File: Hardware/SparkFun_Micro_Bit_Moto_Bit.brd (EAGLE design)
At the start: 58.4 x 76.2 mm, 51 parts, among them J1 POWER_JACKPTH_LOCK, J2 CORTEX_DEBUGPTH, U1 CY8C4245LQI-483, U2 TPS62172, U3 micro:bit, U4 DRV8835

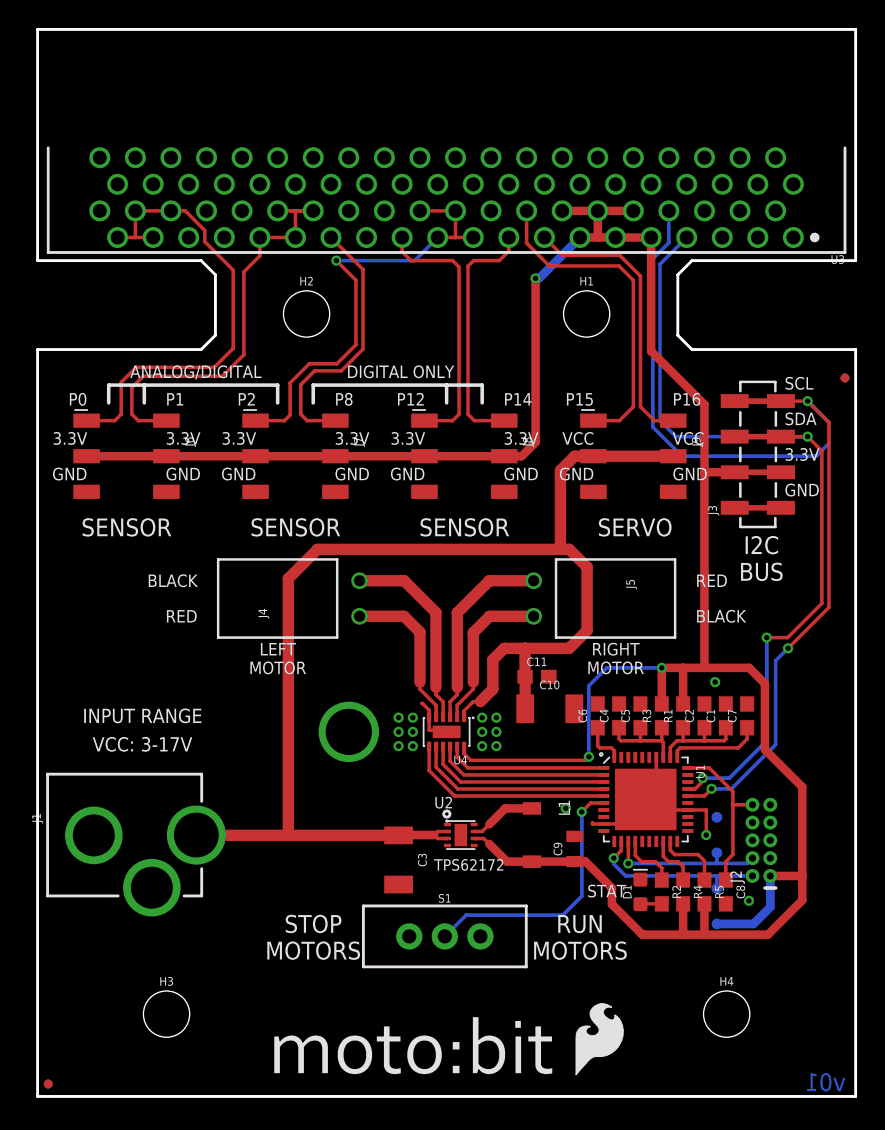
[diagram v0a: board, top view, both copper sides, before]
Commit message: Rounded Corners
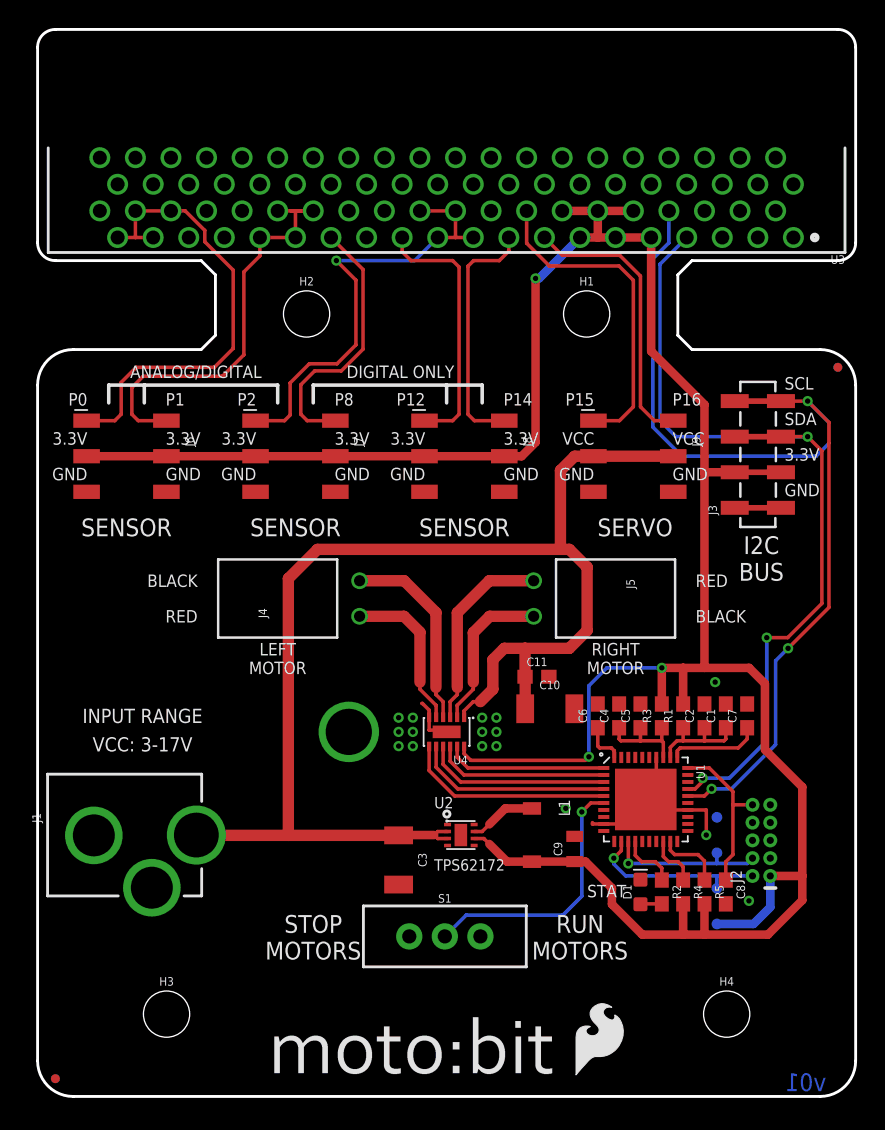
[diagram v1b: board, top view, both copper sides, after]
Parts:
- moved FD2 0.92 mm to (57.1, 52.1)
- moved FD4 0.92 mm to (57.1, 52.1)
- moved FD1 0.64 mm to (1.27, 1.27)
- moved FD3 0.64 mm to (1.27, 1.27)
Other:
- outline, holes or cut-outs redrawn
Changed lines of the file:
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@@
 <layer number="45" name="Holes" color="7" fill="1" visible="yes" active="yes"/>
 <layer number="46" name="Milling" color="3" fill="1" visible="no" active="yes"/>
-<layer number="47" name="Measures" color="7" fill="1" visible="yes" active="yes"/>
+<layer number="47" name="Measures" color="7" fill="1" visible="no" active="yes"/>
 <layer number="48" name="Document" color="7" fill="1" visible="no" active="yes"/>
 <layer number="49" name="Reference" color="7" fill="1" visible="no" active="yes"/>
@@
 <board>
 <plain>
-<wire x1="58.42" y1="0" x2="58.42" y2="53.34" width="0.2032" layer="20"/>
-<wire x1="0" y1="53.34" x2="0" y2="0" width="0.2032" layer="20"/>
+<wire x1="2.54" y1="0" x2="55.88" y2="0" width="0.2032" layer="20"/>
+<wire x1="55.88" y1="0" x2="58.42" y2="2.54" width="0.2032" layer="20" curve="90"/>
+<wire x1="46.736" y1="53.34" x2="55.88" y2="53.34" width="0.2032" layer="20"/>
+<wire x1="55.88" y1="53.34" x2="58.42" y2="50.8" width="0.2032" layer="20" curve="-90"/>
+<wire x1="58.42" y1="50.8" x2="58.42" y2="2.54" width="0.2032" layer="20"/>
+<wire x1="0" y1="2.54" x2="0" y2="50.8" width="0.2032" layer="20"/>
+<wire x1="0" y1="50.8" x2="2.54" y2="53.34" width="0.2032" layer="20" curve="-90"/>
+<wire x1="2.54" y1="53.34" x2="11.684" y2="53.34" width="0.2032" layer="20"/>
+<wire x1="0" y1="2.54" x2="2.54" y2="0" width="0.2032" layer="20" curve="90"/>
 <text x="24.13" y="-31.75" size="1.778" layer="51" font="vector" ratio="15">Alex Wende</text>
-<text x="56.261" y="0.381" size="1.27" layer="16" font="vector" ratio="15" rot="MR0" align="bottom-center">v01</text>
+<text x="54.864" y="0.381" size="1.27" layer="16" font="vector" ratio="15" rot="MR0" align="bottom-center">v01</text>
 <text x="-17.78" y="-49.53" size="1.27" layer="51" font="vector" ratio="15">- Solder mask color : Gloss Black</text>
-<wire x1="0" y1="0" x2="58.42" y2="0" width="0.2032" layer="20"/>
-<wire x1="58.42" y1="59.69" x2="46.736" y2="59.69" width="0.2032" layer="20"/>
+<wire x1="58.42" y1="74.93" x2="58.42" y2="60.96" width="0.2032" layer="20"/>
+<wire x1="58.42" y1="60.96" x2="57.15" y2="59.69" width="0.2032" layer="20" curve="-90"/>
+<wire x1="57.15" y1="59.69" x2="46.736" y2="59.69" width="0.2032" layer="20"/>
 <wire x1="46.736" y1="59.69" x2="45.72" y2="58.674" width="0.2032" layer="20"/>
 <wire x1="45.72" y1="58.674" x2="45.72" y2="54.356" width="0.2032" layer="20"/>
 <wire x1="45.72" y1="54.356" x2="46.736" y2="53.34" width="0.2032" layer="20"/>
-<wire x1="46.736" y1="53.34" x2="58.42" y2="53.34" width="0.2032" layer="20"/>
-<wire x1="0" y1="53.34" x2="11.684" y2="53.34" width="0.2032" layer="20"/>
 <wire x1="11.684" y1="53.34" x2="12.7" y2="54.356" width="0.2032" layer="20"/>
 <wire x1="12.7" y1="54.356" x2="12.7" y2="58.674" width="0.2032" layer="20"/>
 <wire x1="12.7" y1="58.674" x2="11.684" y2="59.69" width="0.2032" layer="20"/>
-<wire x1="11.684" y1="59.69" x2="0" y2="59.69" width="0.2032" layer="20"/>
-<wire x1="0" y1="59.69" x2="0" y2="76.2" width="0.2032" layer="20"/>
-<wire x1="0" y1="76.2" x2="58.42" y2="76.2" width="0.2032" layer="20"/>
-<wire x1="58.42" y1="76.2" x2="58.42" y2="59.69" width="0.2032" layer="20"/>
+<wire x1="11.684" y1="59.69" x2="1.27" y2="59.69" width="0.2032" layer="20"/>
+<wire x1="1.27" y1="59.69" x2="0" y2="60.96" width="0.2032" layer="20" curve="-90"/>
+<wire x1="0" y1="60.96" x2="0" y2="74.93" width="0.2032" layer="20"/>
+<wire x1="0" y1="74.93" x2="1.27" y2="76.2" width="0.2032" layer="20" curve="-90"/>
+<wire x1="1.27" y1="76.2" x2="57.15" y2="76.2" width="0.2032" layer="20"/>
+<wire x1="57.15" y1="76.2" x2="58.42" y2="74.93" width="0.2032" layer="20" curve="-90"/>
 <text x="3.556" y="49.784" size="0.889" layer="21" font="vector" ratio="15" rot="R180" align="center-left">P0</text>
 <text x="9.144" y="49.784" size="0.889" layer="21" font="vector" ratio="15" align="center-left">P1</text>
@@
 <element name="LOGO1" library="SparkFun-Aesthetics" package="SFE_LOGO_NAME_FLAME_.3" value="SFE_LOGO_NAME_FLAME.3_INCH" x="46.99" y="41.91" rot="MR0"/>
 <element name="LOGO2" library="SparkFun-Aesthetics" package="OSHW-LOGO-L" value="OSHW-LOGOL" x="29.083" y="6.477" rot="MR0"/>
-<element name="FD1" library="SparkFun-Aesthetics" package="FIDUCIAL-MICRO" value="FIDUCIALUFIDUCIAL" x="0.762" y="0.889"/>
-<element name="FD2" library="SparkFun-Aesthetics" package="FIDUCIAL-MICRO" value="FIDUCIALUFIDUCIAL" x="57.658" y="51.308"/>
+<element name="FD1" library="SparkFun-Aesthetics" package="FIDUCIAL-MICRO" value="FIDUCIALUFIDUCIAL" x="1.27" y="1.27"/>
+<element name="FD2" library="SparkFun-Aesthetics" package="FIDUCIAL-MICRO" value="FIDUCIALUFIDUCIAL" x="57.15" y="52.07"/>
 <element name="U1" library="SparkFun-IC-Microcontroller" package="QFN-40" value="CY8C4245LQI-483" x="43.434" y="21.209" rot="R270">
 <attribute name="PROD_ID" value="IC-13292" x="-8.636" y="107.569" size="1.778" layer="27" font="vector" ratio="15" rot="R270" display="off"/>
@@
 <element name="H3" library="SparkFun-Hardware" package="STAND-OFF" value="STAND-OFF" x="9.21" y="5.88"/>
 <element name="H4" library="SparkFun-Hardware" package="STAND-OFF" value="STAND-OFF" x="49.21" y="5.88"/>
-<element name="FD3" library="SparkFun-Aesthetics" package="FIDUCIAL-MICRO" value="FIDUCIALUFIDUCIAL" x="0.762" y="0.889" rot="MR0"/>
-<element name="FD4" library="SparkFun-Aesthetics" package="FIDUCIAL-MICRO" value="FIDUCIALUFIDUCIAL" x="57.658" y="51.308" rot="MR0"/>
+<element name="FD3" library="SparkFun-Aesthetics" package="FIDUCIAL-MICRO" value="FIDUCIALUFIDUCIAL" x="1.27" y="1.27" rot="MR0"/>
+<element name="FD4" library="SparkFun-Aesthetics" package="FIDUCIAL-MICRO" value="FIDUCIALUFIDUCIAL" x="57.15" y="52.07" rot="MR0"/>
 <element name="J9" library="SparkFun-Connectors" package="2X3_SMD" value="" x="42.545" y="45.72" rot="R270">
 <attribute name="PROD_ID" value="CONN-11290" x="-100.965" y="190.5" size="1.778" layer="27" font="vector" ratio="15" rot="R270" display="off"/>
@@
 <contactref element="J9" pad="6"/>
 <polygon width="0.254" layer="1" isolate="0.254" rank="2">
-<vertex x="0" y="76.2"/>
-<vertex x="58.42" y="76.2"/>
-<vertex x="58.42" y="59.69"/>
+<vertex x="0" y="60.96"/>
+<vertex x="0" y="74.93" curve="-90"/>
+<vertex x="1.27" y="76.2"/>
+<vertex x="57.15" y="76.2" curve="-90"/>
+<vertex x="58.42" y="74.93"/>
+<vertex x="58.42" y="60.96" curve="-90"/>
+<vertex x="57.15" y="59.69"/>
 <vertex x="46.736" y="59.69"/>
 <vertex x="45.72" y="58.674"/>
 <vertex x="45.72" y="54.356"/>
 <vertex x="46.736" y="53.34"/>
-<vertex x="58.42" y="53.34"/>
-<vertex x="58.42" y="0"/>
-<vertex x="0" y="0"/>
-<vertex x="0" y="53.34"/>
+<vertex x="55.88" y="53.34" curve="-90"/>
+<vertex x="58.42" y="50.8"/>
+<vertex x="58.42" y="2.54" curve="-90"/>
+<vertex x="55.88" y="0"/>
+<vertex x="2.54" y="0" curve="-90"/>
+<vertex x="0" y="2.54"/>
+<vertex x="0" y="50.8" curve="-90"/>
+<vertex x="2.54" y="53.34"/>
 <vertex x="11.684" y="53.34"/>
 <vertex x="12.7" y="54.356"/>
 <vertex x="12.7" y="58.674"/>
 <vertex x="11.684" y="59.69"/>
-<vertex x="0" y="59.69"/>
+<vertex x="1.27" y="59.69" curve="-90"/>
 </polygon>
 <wire x1="40.434" y1="19.459" x2="41.684" y2="19.459" width="0.254" layer="1"/>
@@
 <wire x1="44.184" y1="21.959" x2="43.434" y2="21.209" width="0.254" layer="1"/>
 <polygon width="0.254" layer="16" isolate="0.254" rank="2">
-<vertex x="58.42" y="0"/>
-<vertex x="0" y="0"/>
-<vertex x="0" y="53.34"/>
+<vertex x="46.736" y="53.34"/>
+<vertex x="55.88" y="53.34" curve="-90"/>
+<vertex x="58.42" y="50.8"/>
+<vertex x="58.42" y="2.54" curve="-90"/>
+<vertex x="55.88" y="0"/>
+<vertex x="2.54" y="0" curve="-90"/>
+<vertex x="0" y="2.54"/>
+<vertex x="0" y="50.8" curve="-90"/>
+<vertex x="2.54" y="53.34"/>
 <vertex x="11.684" y="53.34"/>
 <vertex x="12.7" y="54.356"/>
 <vertex x="12.7" y="58.674"/>
 <vertex x="11.684" y="59.69"/>
-<vertex x="0" y="59.69"/>
-<vertex x="0" y="76.2"/>
-<vertex x="58.42" y="76.2"/>
-<vertex x="58.42" y="59.69"/>
+<vertex x="1.27" y="59.69" curve="-90"/>
+<vertex x="0" y="60.96"/>
+<vertex x="0" y="74.93" curve="-90"/>
+<vertex x="1.27" y="76.2"/>
+<vertex x="57.15" y="76.2" curve="-90"/>
+<vertex x="58.42" y="74.93"/>
+<vertex x="58.42" y="60.96" curve="-90"/>
+<vertex x="57.15" y="59.69"/>
 <vertex x="46.736" y="59.69"/>
 <vertex x="45.72" y="58.674"/>
 <vertex x="45.72" y="54.356"/>
-<vertex x="46.736" y="53.34"/>
-<vertex x="58.42" y="53.34"/>
 </polygon>
 <wire x1="40.434" y1="19.459" x2="39.624" y2="19.459" width="0.254" layer="1"/>

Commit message: V10 Changes
- Replaced 2x3 female headers to male
- Changed net label on heatsink mounting hole to GND
- Increased distance between exposed pad and motor connectors
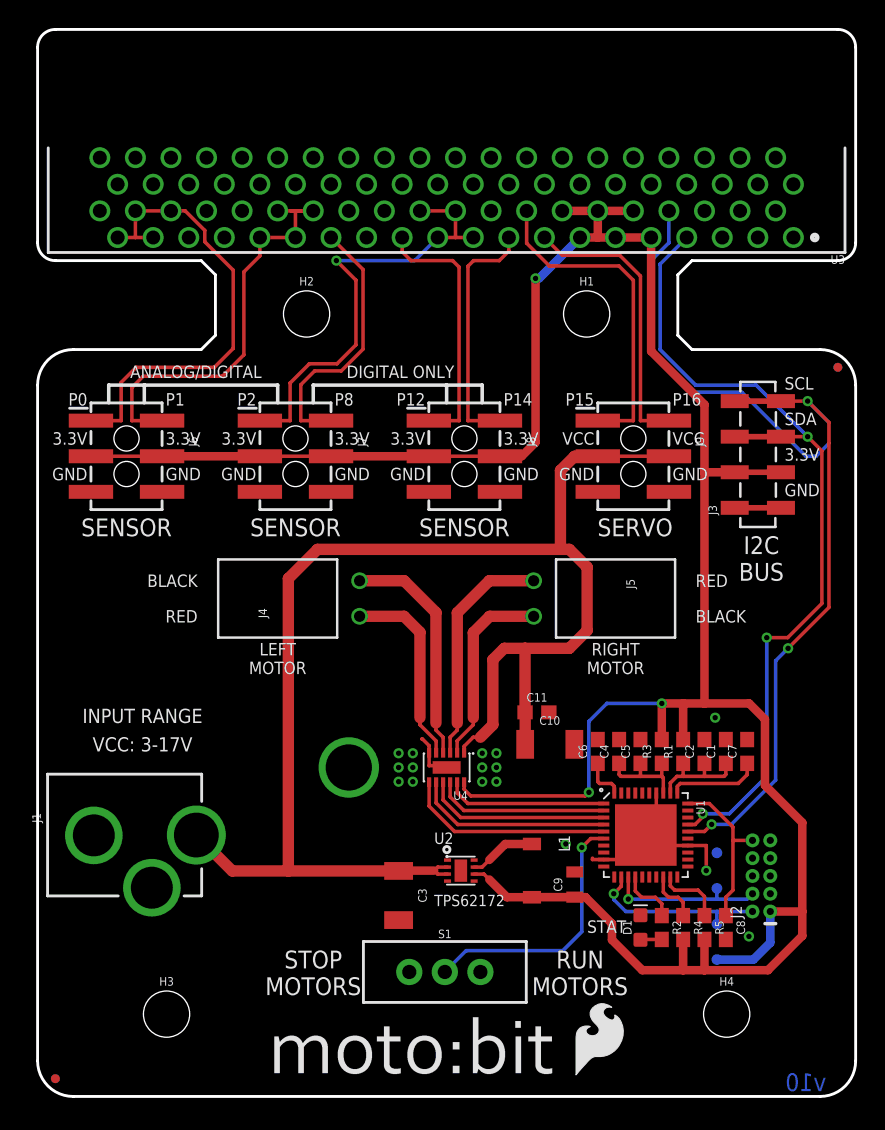
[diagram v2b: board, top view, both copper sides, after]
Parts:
- J6, J7, J8, J9: device SparkFun-Connectors:2X3_SMD -> SparkFun-Connectors:2X3_SMT_POSTS
- moved U$4 7.00 mm to (39.6, 30.6)
- moved LOGO1 6.48 mm to (45.7, 35.6)
- moved LOGO2 6.35 mm to (29.2, 12.8)
- moved C11 2.54 mm to (35.7, 27.4)
- moved C8 2.54 mm to (49.1, 12.1)
- moved D1 2.54 mm to (43.1, 12.1)
- moved J2 2.54 mm to (51.7, 15.7)
- moved R2 2.54 mm to (44.6, 12.1)
- moved R4 2.54 mm to (46.1, 12.1)
- moved R5 2.54 mm to (47.6, 12.1)
- moved TP2 2.54 mm to (48.5, 14.9)
- moved TP3 2.54 mm to (48.5, 9.78)
- moved C1 2.54 mm to (49.1, 24.6)
- moved C10 2.54 mm to (36.6, 25.1)
- moved C2 2.54 mm to (47.6, 24.6)
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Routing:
- net VCC: track 96.0 -> 104.4 mm
- net BO2: track 11.3 -> 13.9 mm
- net BO1: track 14.1 -> 16.6 mm
- net AO2: track 14.1 -> 16.6 mm
- net AO1: track 11.3 -> 13.8 mm
- net 3.3V: track 186.4 -> 188.6 mm
- net SCL: track 73.1 -> 72.6 mm
- net GND: vias 16 -> 17
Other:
- board text added: "v10"
- board text removed: "v01"
